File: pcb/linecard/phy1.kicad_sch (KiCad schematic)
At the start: 34 parts, among them J11 SMPM, J12 SMPM, J13 XILINX_JTAG, J14 ARF6-08-S-D-A-K-TR, M13 960-27-12-D-AB-0, U35 VSC8512, U61 SIT9121AC-2B2-33E125.000000

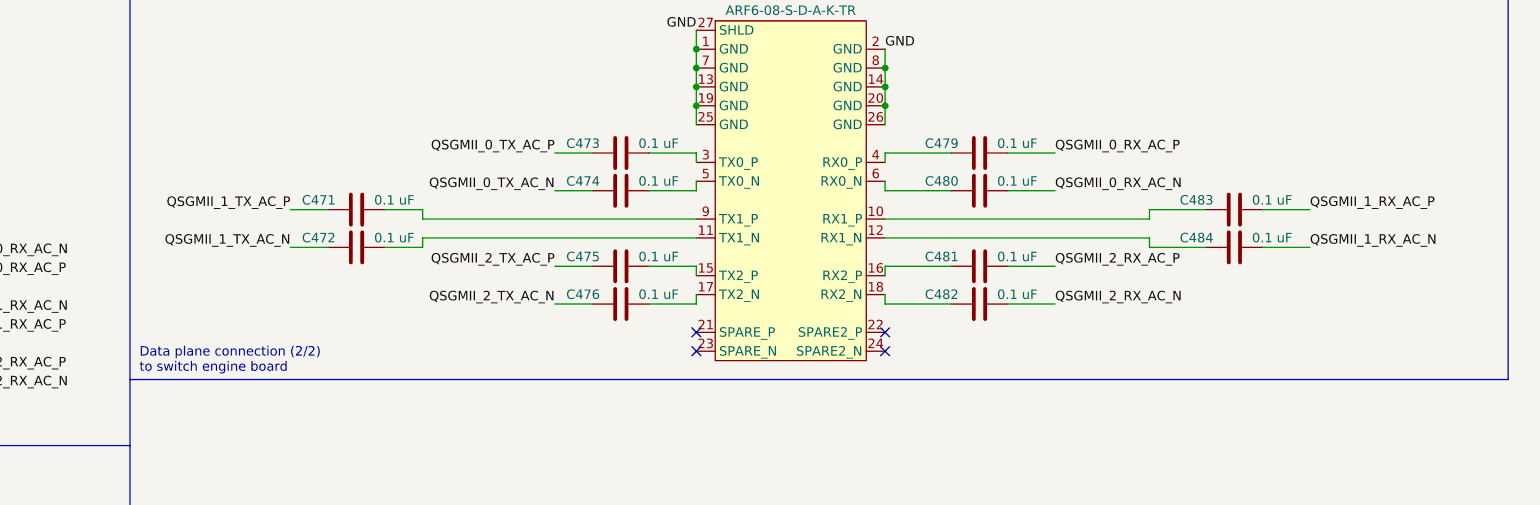
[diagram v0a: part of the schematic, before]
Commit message: Continued tying up loose ends on routing of left side and supervisor
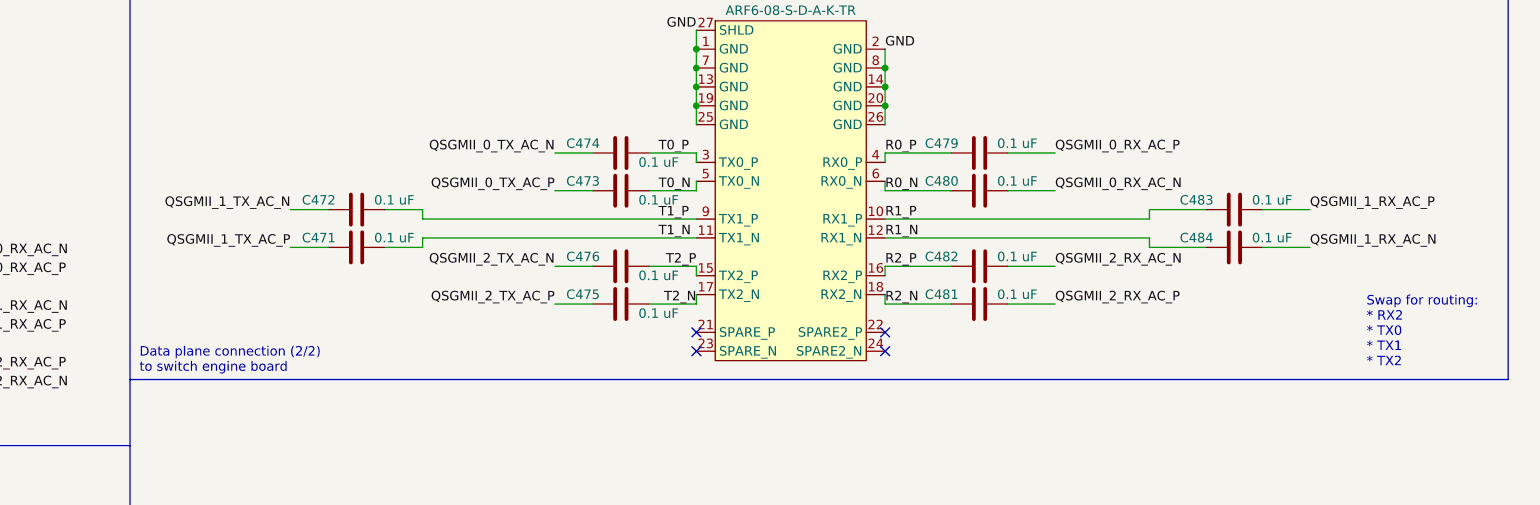
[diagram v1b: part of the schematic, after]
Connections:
- net R1_N: now reaches C484.1, J14.12 (RX1_N)
- net R2_N: now reaches J14.18 (RX2_N)
- net R2_N: now also C481.1; no longer C482.1
- net R0_N: now reaches C480.1, J14.6 (RX0_N)
- net R0_P: now reaches C479.1, J14.4 (RX0_P)
- net T1_N: now reaches C471.2
- net T1_N: now also J14.11 (TX1_N); no longer J14.9 (TX1_P)
- net T2_N: now reaches J14.17 (TX2_N)
- net T2_N: now also C475.2; no longer C476.2
- net T1_P: now reaches C472.2
- net T1_P: now also J14.9 (TX1_P); no longer J14.11 (TX1_N)
- net T2_P: now reaches J14.15 (TX2_P)
- net T2_P: now also C476.2; no longer C475.2
- net R1_P: now reaches C483.1, J14.10 (RX1_P)
- net T0_N: now reaches C473.2
- net T0_N: now also J14.5 (TX0_N); no longer J14.3 (TX0_P)
- net R2_P: now reaches J14.16 (RX2_P)
- net R2_P: now also C482.1; no longer C481.1
- net T0_P: now reaches C474.2
- net T0_P: now also J14.3 (TX0_P); no longer J14.5 (TX0_N)
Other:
- note added: "Swap for routing: * RX2 * TX0 * TX1 * TX2"
- moved on the sheet: C471, C472, C473, C474, C475, C476, C481, C482

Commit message: Added planes, more LED signals, etc
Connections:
- net REFCLK_N: now also C477.1; no longer C478.1
- net REFCLK_P: now also C478.1; no longer C477.1
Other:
- moved on the sheet: C477, C478
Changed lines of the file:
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@@
 	)
 	(label "REFCLK_AC_N"
-		(at 198.12 276.86 0)
+		(at 198.12 266.7 0)
 		(fields_autoplaced yes)
 		(effects
@@
 	)
 	(label "REFCLK_AC_P"
-		(at 198.12 266.7 0)
+		(at 198.12 276.86 0)
 		(fields_autoplaced yes)
 		(effects
@@
 	(symbol
 		(lib_id "device:C")
-		(at 194.31 276.86 90)
+		(at 194.31 266.7 90)
 		(unit 1)
 		(exclude_from_sim no)
@@
 		(fields_autoplaced yes)
 		(property "Reference" "C478"
-			(at 194.31 271.0012 90)
+			(at 194.31 260.8412 90)
 			(effects
 				(font
@@
 		)
 		(property "Value" "0.1 uF"
-			(at 194.31 273.5381 90)
+			(at 194.31 263.3781 90)
 			(effects
 				(font
@@
 		)
 		(property "Footprint" "azonenberg_pcb:EIA_0402_CAP_NOSILK"
-			(at 198.12 275.8948 0)
+			(at 198.12 265.7348 0)
 			(effects
 				(font
@@
 		)
 		(property "Datasheet" ""
-			(at 194.31 276.86 0)
+			(at 194.31 266.7 0)
 			(effects
 				(font
@@
 		)
 		(property "Description" ""
-			(at 194.31 276.86 0)
+			(at 194.31 266.7 0)
 			(effects
 				(font
@@
 	(symbol
 		(lib_id "device:C")
-		(at 194.31 266.7 90)
+		(at 194.31 276.86 90)
 		(unit 1)
 		(exclude_from_sim no)
@@
 		(fields_autoplaced yes)
 		(property "Reference" "C477"
-			(at 194.31 260.8412 90)
+			(at 194.31 271.0012 90)
 			(effects
 				(font
@@
 		)
 		(property "Value" "0.1 uF"
-			(at 194.31 263.3781 90)
+			(at 194.31 273.5381 90)
 			(effects
 				(font
@@
 		)
 		(property "Footprint" "azonenberg_pcb:EIA_0402_CAP_NOSILK"
-			(at 198.12 265.7348 0)
+			(at 198.12 275.8948 0)
 			(effects
 				(font
@@
 		)
 		(property "Datasheet" ""
-			(at 194.31 266.7 0)
+			(at 194.31 276.86 0)
 			(effects
 				(font
@@
 		)
 		(property "Description" ""
-			(at 194.31 266.7 0)
+			(at 194.31 276.86 0)
 			(effects
 				(font
